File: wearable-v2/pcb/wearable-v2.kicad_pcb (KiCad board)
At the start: 2 copper layers, 112.1 x 40.2 mm, 86 parts, among them IC1 TESEO-LIV3F, J1 HERALD_V2_CONN_RECEPTACLE, J2 HERALD_V2_CONN_RECEPTACLE, J3 HERALD_V2_CONN_RECEPTACLE, J4 HERALD_V2_CONN_RECEPTACLE, J7 USB_C_Receptacle_USB2.0, SW1 SW_Push, U1 DT1446-04V, U10 ATmega328PB-M, U11 TMP1075, U12 MAX30102, U14 LIS2DE12, U15 TLV751, U2 MCP73831/2-2MC, U3 TCA6408A, U4 FT201XQ, U6 BC833, U7 MX25R8035FZxxx0, U8 PCF85063ATL, U9 APDS-9250, Y1 32.768kHz

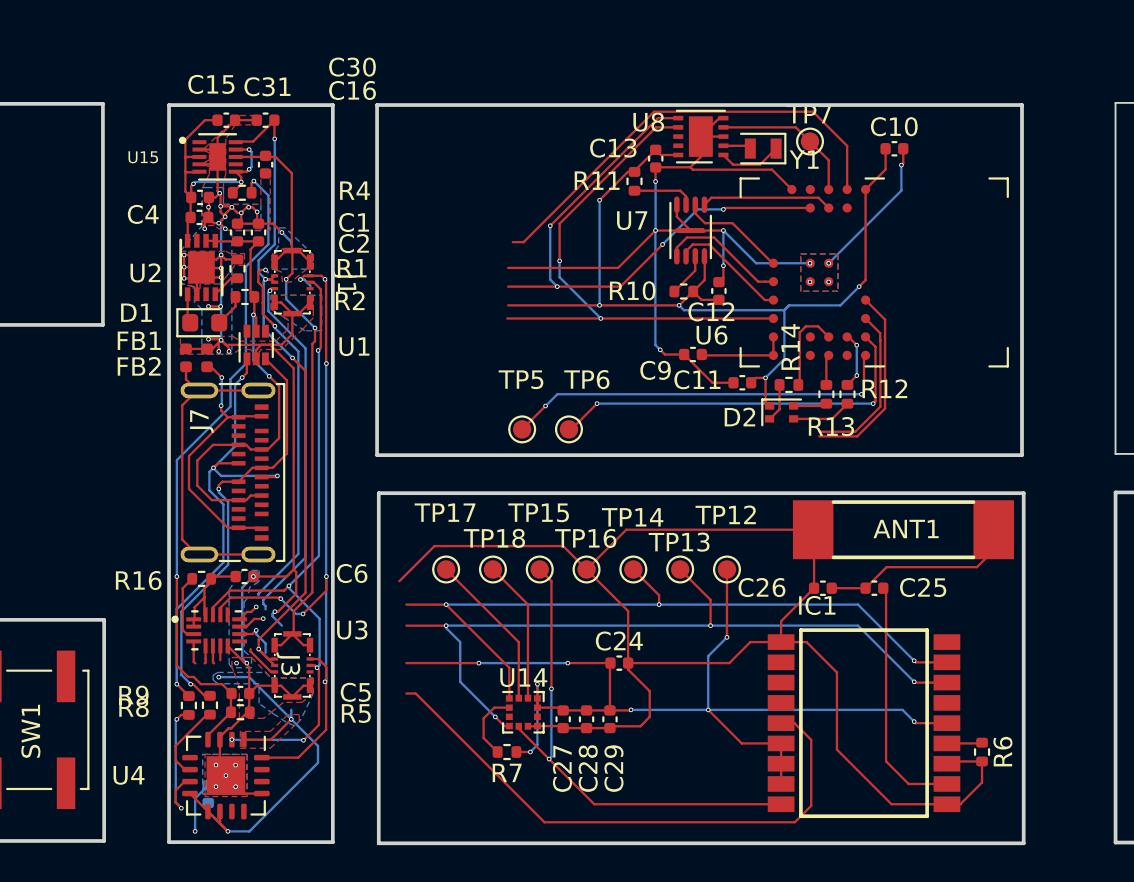
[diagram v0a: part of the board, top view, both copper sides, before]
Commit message: Added plug connector and routed compute and positioning boards
Signed-off-by: Adam Fowler <adam@adamfowler.org>
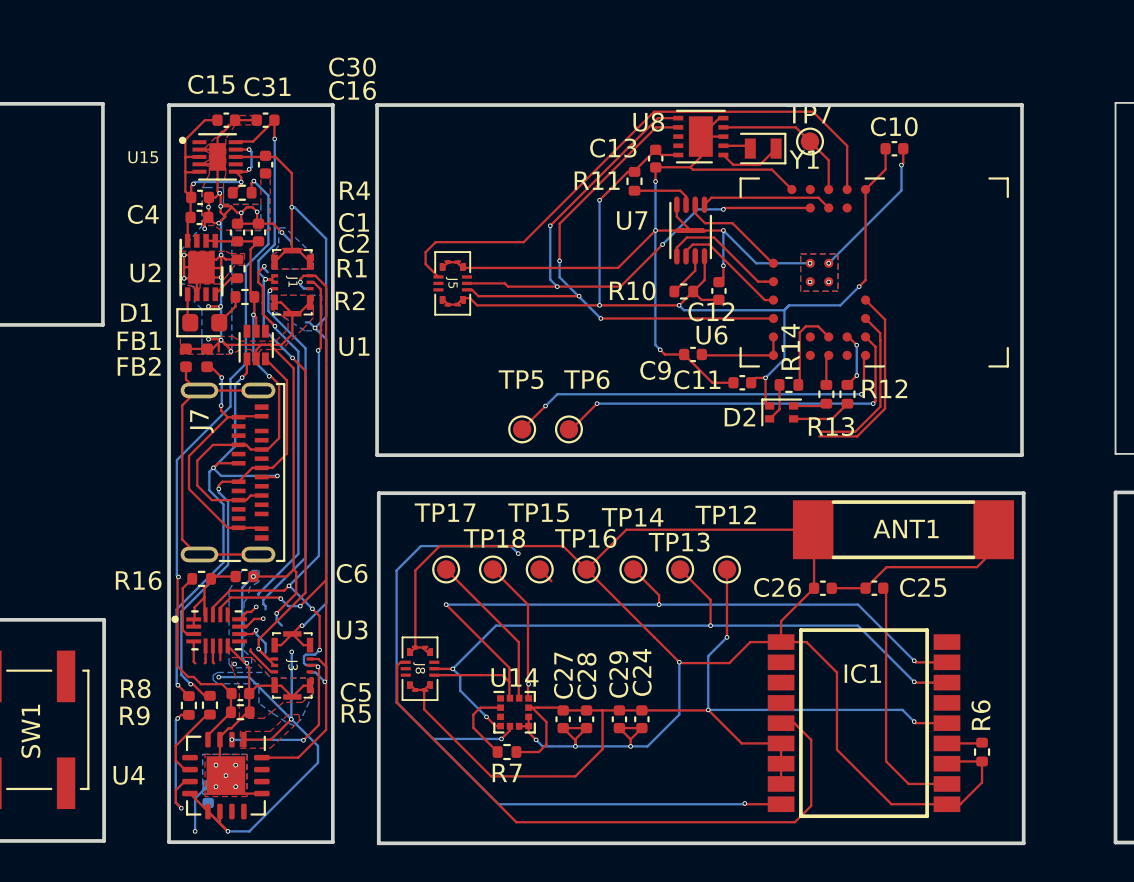
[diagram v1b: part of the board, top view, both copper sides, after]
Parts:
- added J5: HERALD_V2_CONN_PORT, Herald:HERALD_V2_CONN_PORT, F.Cu at (106.7, 108.9)
- added J8: HERALD_V2_CONN_PORT, Herald:HERALD_V2_CONN_PORT, F.Cu at (104.9, 129.8)
- moved C24 3.28 mm to (116.9, 132.6), turned to -90 degrees
- moved C29 0.51 mm to (115.7, 132.6)
- moved U14 0.48 mm to (110.0, 132.2)
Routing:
- net GND: track 277.3 -> 293.9 mm, vias 51 -> 48
- net /Positioning Board V1/POS_RESETn: track 26.7 -> 43.2 mm, vias 2 -> 3
- net VDD: track 219.8 -> 232.5 mm, vias 23 -> 21
- net /Compute - Fanstel BC833M - Nordic Semi nRF52833 based/EXT_INT1: track 43.8 -> 50.4 mm
- net /Bio Board V1/SCL: track 138.0 -> 141.4 mm, vias 15 -> 13
- net /Positioning Board V1/GNSS_INT: track 34.2 -> 37.1 mm
- net /Bio Board V1/SDA: track 139.9 -> 140.3 mm, vias 16 -> 18

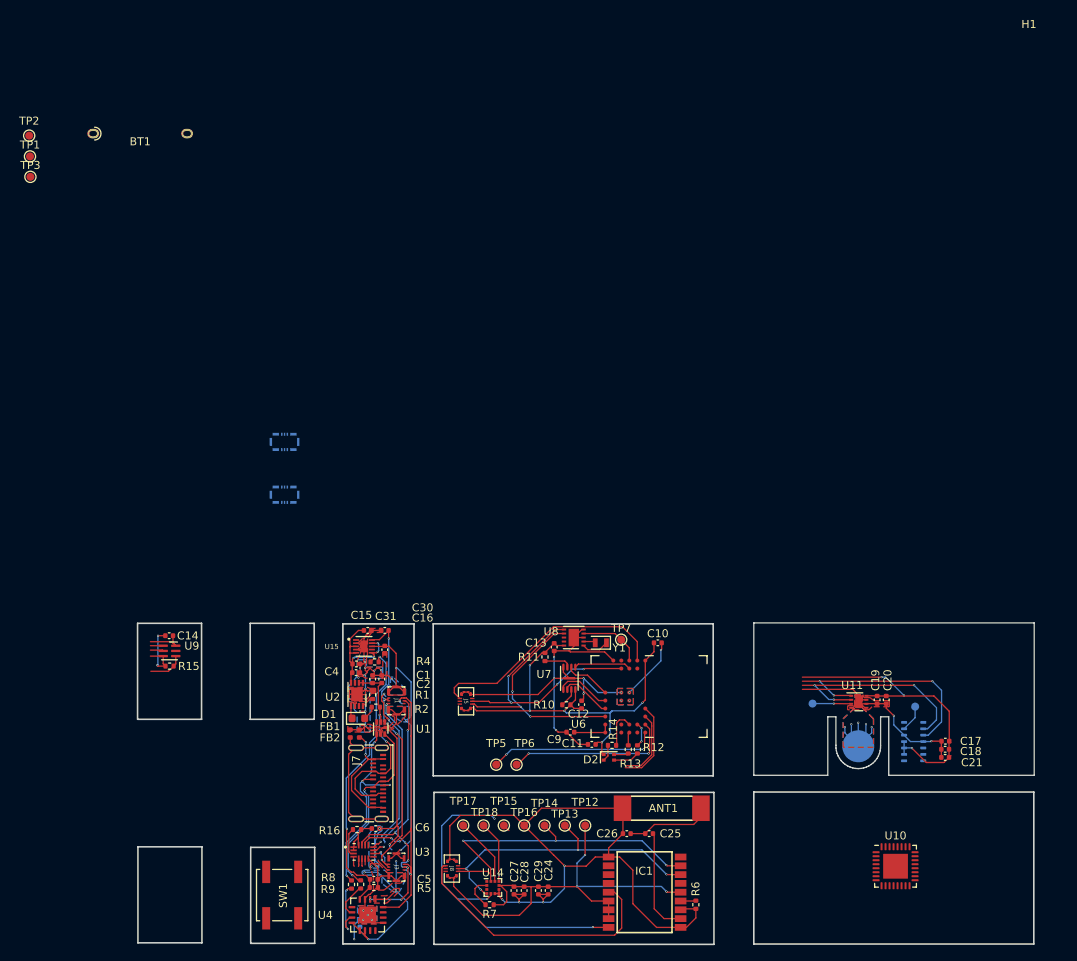
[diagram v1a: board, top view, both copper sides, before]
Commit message: All board connectors routed
Connector positions confirmed
Extension board dimensions confirmed to not clash
Signed-off-by: Adam Fowler <adam@adamfowler.org>
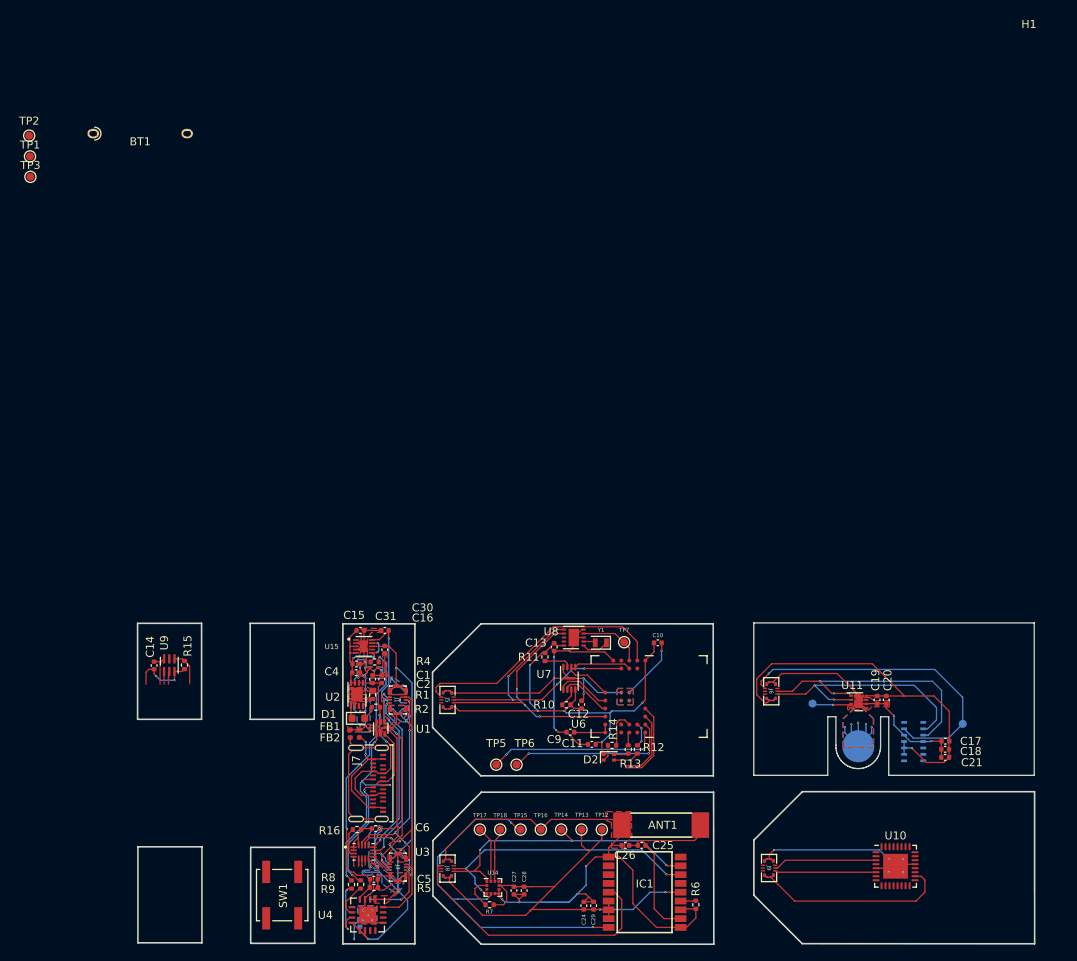
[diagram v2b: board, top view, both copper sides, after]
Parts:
- added J6: HERALD_V2_CONN_PORT, Herald:HERALD_V2_CONN_PORT, F.Cu at (144.8, 107.7)
- added J9: HERALD_V2_CONN_PORT, Herald:HERALD_V2_CONN_PORT, F.Cu at (144.6, 129.8)
- moved J4 48.7 mm to (98.1, 129.7), turned to 90 degrees
- moved J2 35.2 mm to (98.1, 108.8), turned to 90 degrees
- moved C29 7.15 mm to (122.6, 134.5), turned to 90 degrees
- moved TP11 6.32 mm to (168.8, 111.8)
- moved C24 4.84 mm to (121.4, 134.5), turned to 90 degrees
- moved C14 4.17 mm to (67.7, 104.5), turned to 90 degrees
- moved J5 2.33 mm to (104.4, 108.8)
- moved TP13 2.15 mm to (121.1, 125.0)
- moved TP17 2.15 mm to (108.4, 125.0)
- moved TP12 2.15 mm to (123.6, 125.0)
- moved TP14 2.15 mm to (118.6, 125.0)
- moved TP15 2.15 mm to (113.5, 125.0)
- moved TP16 2.15 mm to (116.0, 125.0)
- moved TP18 2.15 mm to (110.9, 125.0)
- moved ANT1 2.11 mm to (131.1, 124.4)
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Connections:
- ANT1 pad 2: (no net) -> GND
- J2 pad 2: VDD -> 1V8
- J2 pad 4: VDD -> 1V8
- J4 pad 2: VDD -> 1V8
- J4 pad 4: VDD -> 1V8
- U3 pad 10: /Bio Board V1/INT_2 -> /Display Board V1/INT_4
- U3 pad 11: /Positioning Board V1/GNSS_INT -> /Compute - Fanstel BC833M - Nordic Semi nRF52833 based/EXT_INT1
- U3 pad 12: /Display Board V1/INT_4 -> /Bio Board V1/INT_2
- U3 pad 9: /Compute - Fanstel BC833M - Nordic Semi nRF52833 based/EXT_INT1 -> /Positioning Board V1/GNSS_INT
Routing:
- net VDD: track 232.5 -> 287.1 mm, vias 21 -> 17
- net /Bio Board V1/BIO_INT: track 3.34 -> 40.2 mm, vias 0 -> 1
- net GND: track 293.9 -> 330.4 mm, vias 48 -> 53
- net /Bio Board V1/SDA: track 140.3 -> 158.9 mm
- net /Bio Board V1/SCL: track 141.4 -> 155.1 mm, vias 13 -> 12
- net /Compute - Fanstel BC833M - Nordic Semi nRF52833 based/EXT_INT1: track 50.4 -> 54.4 mm, vias 1 -> 2
- net 1V8: track 37.3 -> 40.8 mm
- net /Positioning Board V1/POS_RESETn: track 43.2 -> 45.2 mm
- net /Display Board V1/INT_4: track 1.18 -> 2.81 mm
- net /Positioning Board V1/ACC_INT1: track 8.62 -> 7.05 mm
- net /Positioning Board V1/ANT_RF: track 13.3 -> 12.2 mm
- net /Positioning Board V1/ACC_INT2: track 7.77 -> 6.88 mm
- net Net-(ANT1-Pad1): track 10.8 -> 9.90 mm
- net /Positioning Board V1/GNSS_INT: vias 1 -> 0
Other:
- outline, holes or cut-outs redrawn
- board text added: "NOTE: ALL BUTTON CONNECTORS CONNECT AT LOWER EDGE OF WEARABLE SO THE DISPLAY CAN BE ROTATED DOWNWARDS TO ACCESS THE INNER CIRCUITRY"

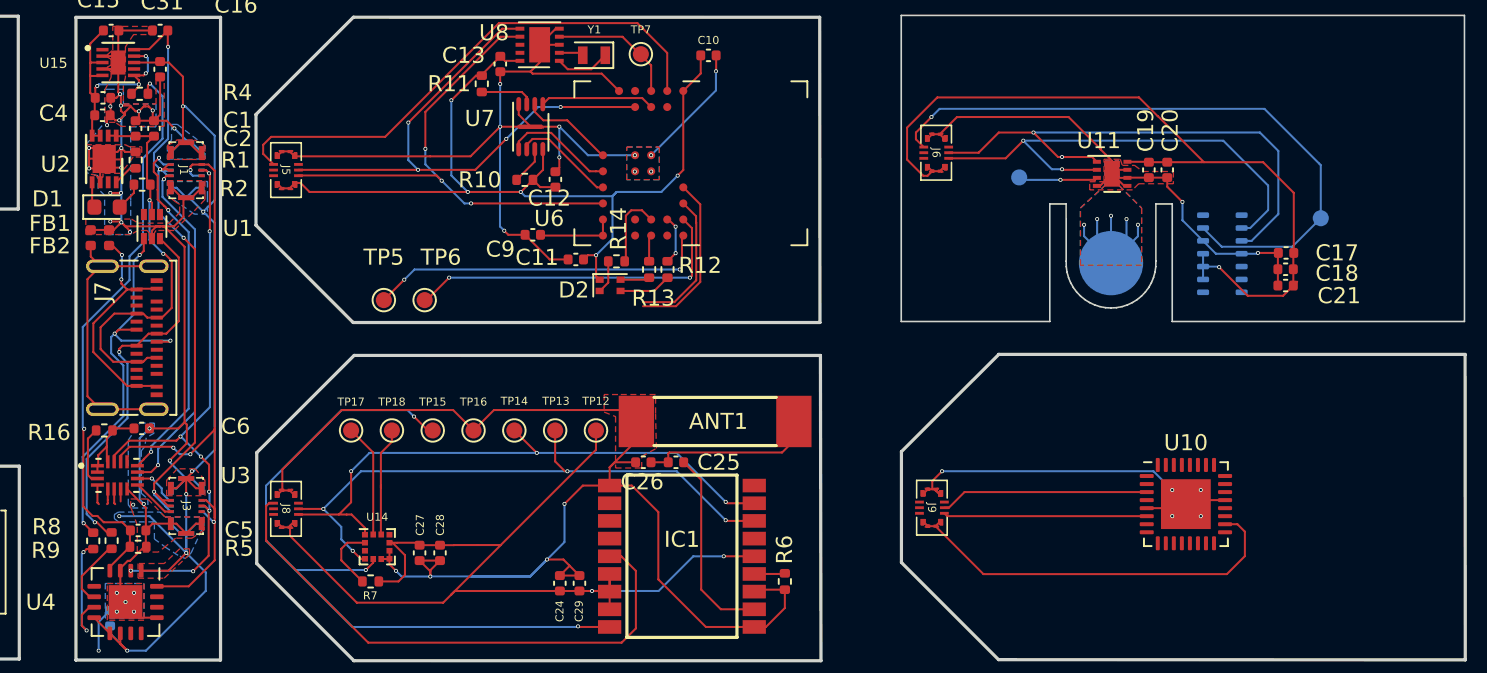
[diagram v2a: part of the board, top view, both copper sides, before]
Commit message: Corrected 1V8 routing to bio board
Signed-off-by: Adam Fowler <adam@adamfowler.org>
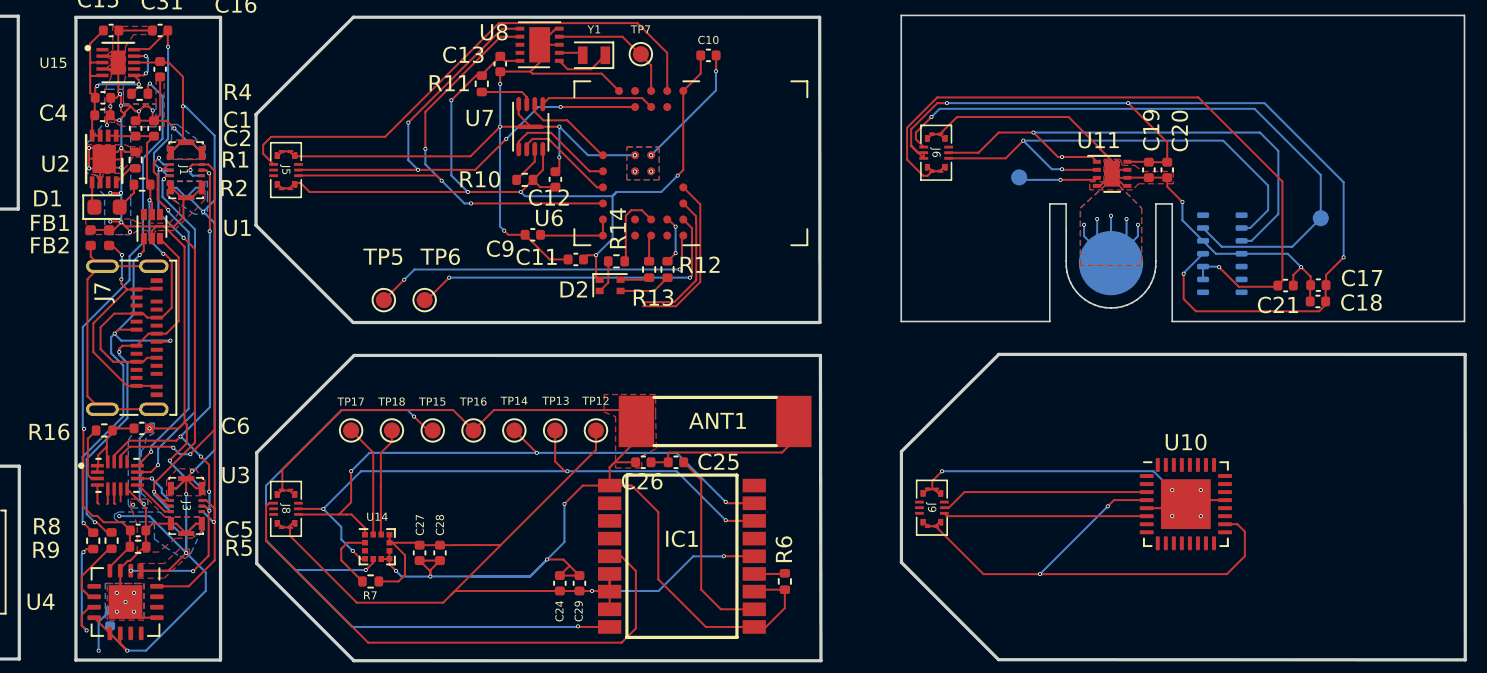
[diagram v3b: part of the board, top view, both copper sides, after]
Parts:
- moved C17 2.84 mm to (168.6, 115.9)
- moved C18 2.84 mm to (168.6, 116.9)
- turned C21 to 0 degrees
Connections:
- C17 pad 1: VDD -> +1V8
- C18 pad 1: VDD -> +1V8
- C19 pad 2: VDD -> +1V8
- C20 pad 2: VDD -> +1V8
- C31 pad 2: 1V8 -> +1V8
- J1 pad 2: 1V8 -> +1V8
- J1 pad 4: 1V8 -> +1V8
- J2 pad 2: 1V8 -> +1V8
- J2 pad 4: 1V8 -> +1V8
- J3 pad 2: 1V8 -> +1V8
- J3 pad 4: 1V8 -> +1V8
- J4 pad 2: 1V8 -> +1V8
- J4 pad 4: 1V8 -> +1V8
- J6 pad 2: (no net) -> +1V8
- J6 pad 4: (no net) -> +1V8
- SW1 pad 1: VDD -> +1V8
- U11 pad 8: VDD -> +1V8
- U12 pad 11: VDD -> +1V8
- U15 pad 10: 1V8 -> +1V8
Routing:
- net +1V8: track 0.00 -> 102.0 mm, vias 0 -> 8
- net 1V8: track 40.8 -> 0.00 mm, vias 4 -> 0
- net GND: track 330.4 -> 333.8 mm
- net VDD: track 287.1 -> 288.7 mm, vias 17 -> 19
